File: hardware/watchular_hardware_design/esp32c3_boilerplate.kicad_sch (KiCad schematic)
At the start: 26 parts, among them J1 USB4105-GF-A, U1 ESP32-C3FH4, U2 MIC5524-3.3YMT-TZ, U3 W25Q16JVSSIQ, Y1 40MHz

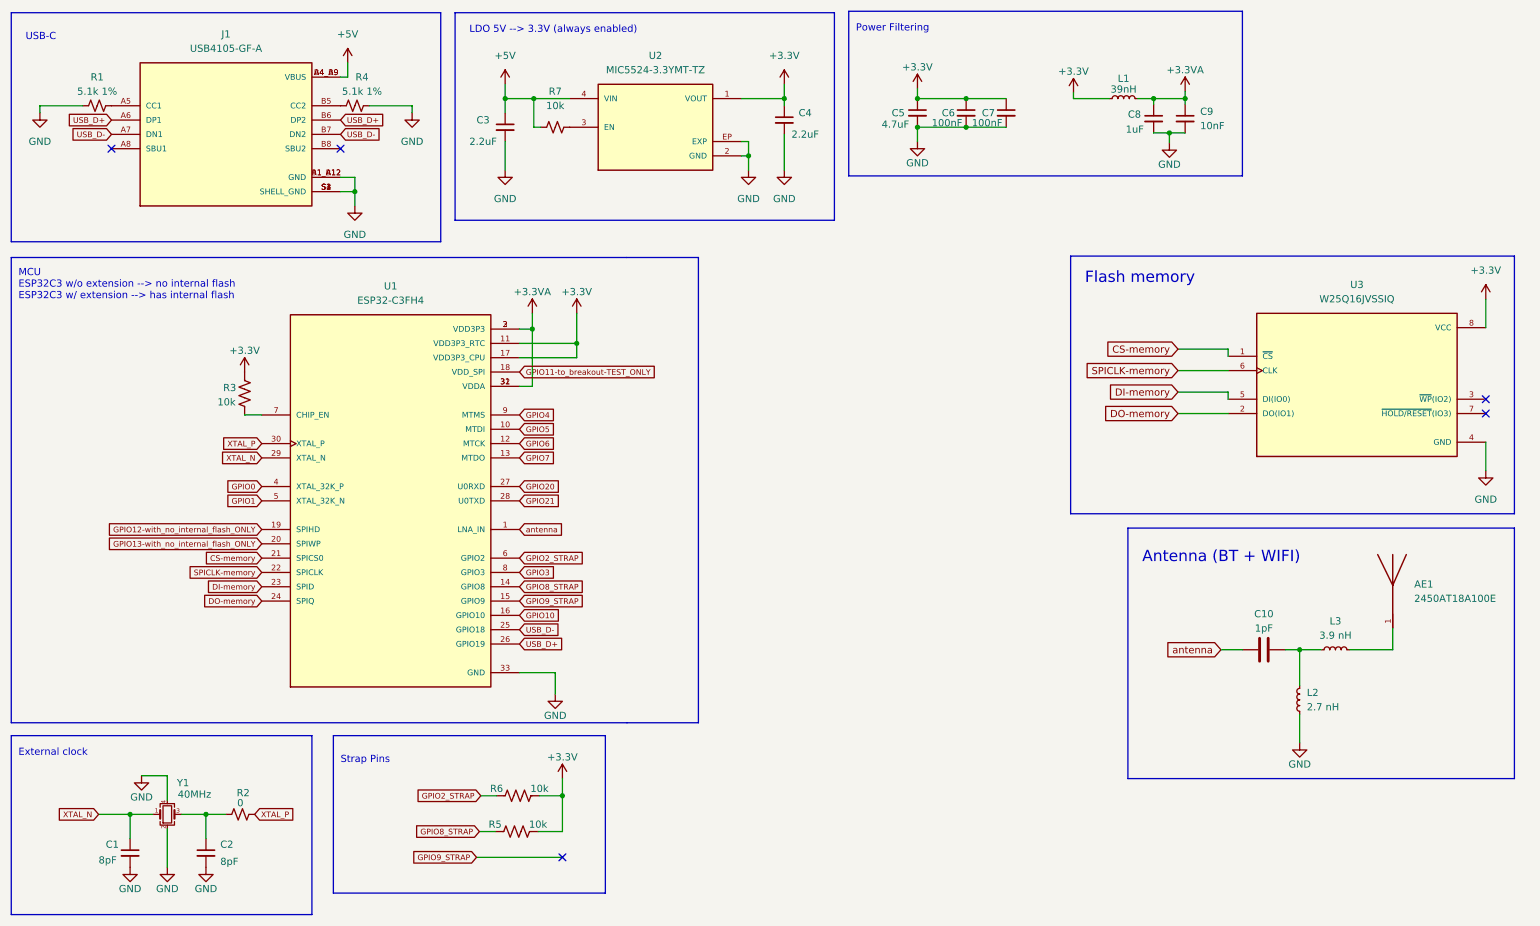
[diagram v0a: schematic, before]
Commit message: Added ESD protection on the USB.
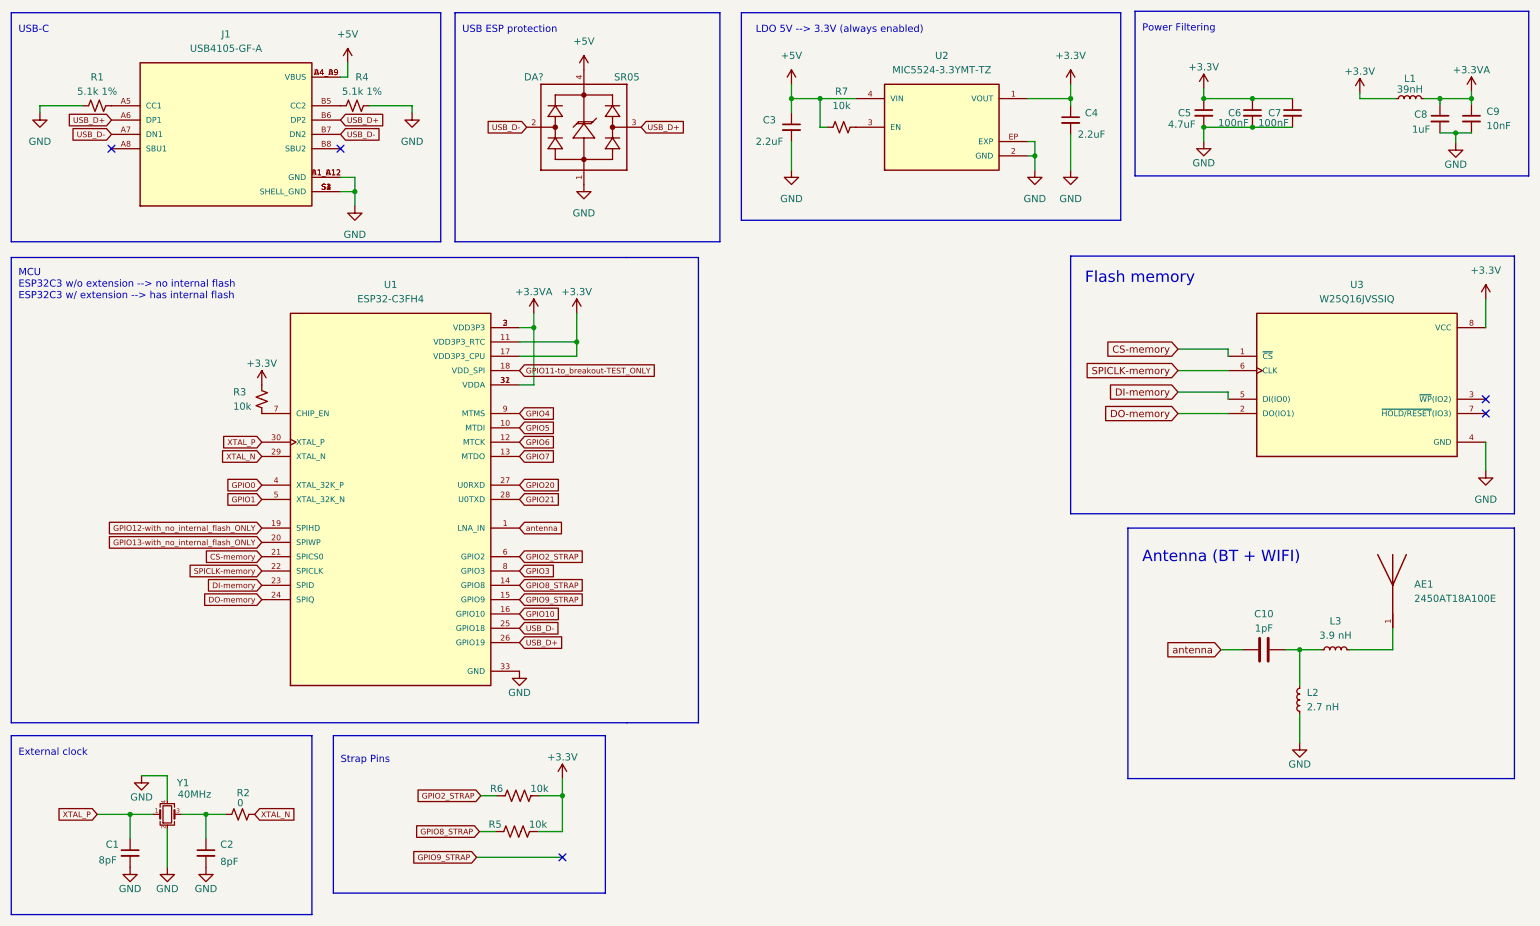
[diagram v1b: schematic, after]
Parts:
- removed R3: 10k, Resistor_SMD:R_0402_1005Metric, symbol Device:R_US
- added DA?: SR05, ESD_protection-SR05:SOT143, symbol SR05:SR05
- added R3: 10k, Resistor_SMD:R_01005_0402Metric_Pad0.57x0.30mm_HandSolder, symbol Device:R_Small_US
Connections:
- net +3V3: now also R3.1
- net +5V: now also DA?.4
- net GND: now also DA?.1
- net USB_D+: now also DA?.3
- net USB_D-: now also DA?.2
- net XTAL_N: now also R2.2; no longer C1.1, Y1.1
- net XTAL_P: now also C1.1, Y1.1; no longer R2.2
- net at U1.7 (CHIP_EN): now also R3.2
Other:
- note added: "USB ESP protection"
- moved on the sheet: C3, C4, C5, C6, C7, C8, C9, L1, R7, U2

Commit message: Coppied to another git repo. Ready to merge.
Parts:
- gave numbers to parts that had none: 1
- renumbered C9 to C10, C10 to C7, C7 to C8, C8 to C9, L2 to L1, L3 to L2, L1 to L3
